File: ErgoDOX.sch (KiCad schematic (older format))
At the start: 62 parts, among them J1 USB, J2 3.5mm, J3 JMP, J4 JMP, SW0:10 SW0:3, SW0:11 SW0:2, SW0:12 SW0:1, SW0:7 SW0:6, SW0:8 SW0:5, SW0:9 SW0:4, SW1:10 SW1:3, SW1:11 SW1:2, SW1:12 SW1:1, SW1:13 SW1:0, SW1:9 SW1:4, SW2:10 SW2:3, SW2:11 SW2:2, SW2:12 SW2:1, SW2:13 SW2:0, SW2:7 SW2:6, SW2:8 SW2:5, SW2:9 SW2:4, SW3:10 SW3:3, SW3:11 SW3:2, SW3:12 SW3:1, SW3:13 SW3:0, SW3:8 SW3:5, SW3:9 SW3:4, SW4:10 SW4:3, SW4:11 SW4:2, SW4:12 SW4:1, SW4:13 SW4:0, SW4:7 SW4:6, SW4:8 SW4:5, SW4:9 SW4:4, SW5:10 SW5:3, SW5:11 SW5:2, SW5:12 SW5:1, SW5:13 SW5:0, SW5:7 SW5:6, SW5:8 SW5:5, SW5:9 SW5:4, U1 ProMicro, U2 MCP23017

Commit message: ...
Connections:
- net VCC: now also U1.26 (VCC); no longer U1.29 (RAW)
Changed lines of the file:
@@
 EESchema Schematic File Version 2
-LIBS:ErgoDOX-rescue
 LIBS:component
 LIBS:74xgxx
@@
 L VCC #PWR015
 U 1 1 500D1293
-P 1950 1300
-F 0 "#PWR015" H 1950 1400 30  0001 C CNN
-F 1 "VCC" H 1950 1400 30  0000 C CNN
-F 2 "" H 1950 1300 60  0001 C CNN
-F 3 "" H 1950 1300 60  0001 C CNN
-	1    1950 1300
-	0    1    1    0
+P 750 3000
+F 0 "#PWR015" H 750 3100 30  0001 C CNN
+F 1 "VCC" H 750 3100 30  0000 C CNN
+F 2 "" H 750 3000 60  0001 C CNN
+F 3 "" H 750 3000 60  0001 C CNN
+	1    750  3000
+	0    -1   -1   0
 $EndComp
 $Comp
@@
 	1    0    0    -1
 $EndComp
-NoConn ~ 750  3000
+NoConn ~ 1950 1300
 $Comp
 L C C1

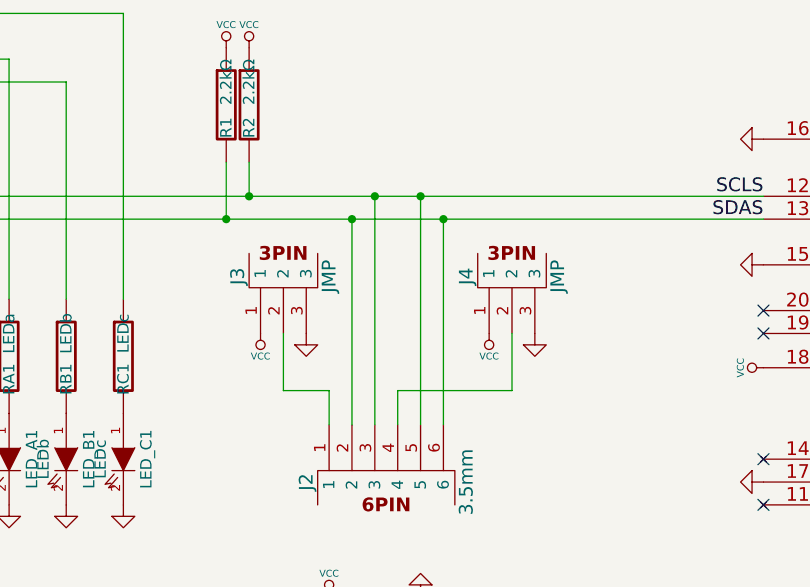
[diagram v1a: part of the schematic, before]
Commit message: Change pin order of 3.5mm jack
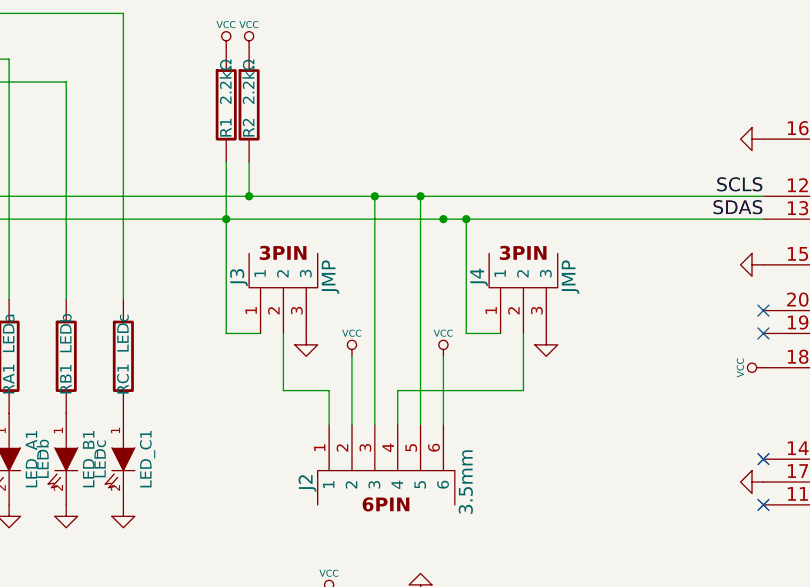
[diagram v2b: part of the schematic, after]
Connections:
- net SDAM: now also J3.1, J4.1; no longer J2.2, J2.6
- net VCC: now also J2.2, J2.6; no longer J3.1, J4.1
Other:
- moved on the sheet: J4
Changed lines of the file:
@@
 L GND #PWR09
 U 1 1 4FD9EC71
-P 5450 3050
-F 0 "#PWR09" H 5450 3050 30  0001 C CNN
-F 1 "GND" H 5450 2980 30  0001 C CNN
-F 2 "" H 5450 3050 60  0001 C CNN
-F 3 "" H 5450 3050 60  0001 C CNN
-	1    5450 3050
+P 5500 3050
+F 0 "#PWR09" H 5500 3050 30  0001 C CNN
+F 1 "GND" H 5500 2980 30  0001 C CNN
+F 2 "" H 5500 3050 60  0001 C CNN
+F 3 "" H 5500 3050 60  0001 C CNN
+	1    5500 3050
 	1    0    0    -1
 $EndComp
 $Comp
 L VCC #PWR010
-U 1 1 4FD9EC77
-P 4250 3000
-F 0 "#PWR010" H 4250 3100 30  0001 C CNN
-F 1 "VCC" H 4250 3100 30  0000 C CNN
-F 2 "" H 4250 3000 60  0001 C CNN
-F 3 "" H 4250 3000 60  0001 C CNN
-	1    4250 3000
-	-1   0    0    1
-$EndComp
-$Comp
-L VCC #PWR011
 U 1 1 4FD9EC7D
-P 5250 3000
-F 0 "#PWR011" H 5250 3100 30  0001 C CNN
-F 1 "VCC" H 5250 3100 30  0000 C CNN
-F 2 "" H 5250 3000 60  0001 C CNN
-F 3 "" H 5250 3000 60  0001 C CNN
-	1    5250 3000
-	-1   0    0    1
+P 4650 3100
+F 0 "#PWR010" H 4650 3200 30  0001 C CNN
+F 1 "VCC" H 4650 3200 30  0000 C CNN
+F 2 "" H 4650 3100 60  0001 C CNN
+F 3 "" H 4650 3100 60  0001 C CNN
+	1    4650 3100
+	1    0    0    -1
 $EndComp
 $Comp
@@
 L 3PIN J4
 U 1 1 4FD9F052
-P 5350 2800
-F 0 "J4" H 5300 3000 60  0000 C CNN
-F 1 "JMP" H 5300 2600 60  0000 C CNN
-F 2 "" H 5350 2800 60  0001 C CNN
-F 3 "" H 5350 2800 60  0001 C CNN
-	1    5350 2800
+P 5400 2800
+F 0 "J4" H 5350 3000 60  0000 C CNN
+F 1 "JMP" H 5350 2600 60  0000 C CNN
+F 2 "" H 5400 2800 60  0001 C CNN
+F 3 "" H 5400 2800 60  0001 C CNN
+	1    5400 2800
 	0    -1   1    0
 $EndComp
@@
 $EndComp
 $Comp
-L VCC #PWR012
+L VCC #PWR011
 U 1 1 4FFF4300
 P 4550 4150
-F 0 "#PWR012" H 4550 4250 30  0001 C CNN
+F 0 "#PWR011" H 4550 4250 30  0001 C CNN
 F 1 "VCC" H 4550 4250 30  0000 C CNN
 F 2 "" H 4550 4150 60  0001 C CNN
@@
 $EndComp
 $Comp
-L GND #PWR013
+L GND #PWR012
 U 1 1 4FFF43E7
 P 4950 4100
-F 0 "#PWR013" H 4950 4100 30  0001 C CNN
+F 0 "#PWR012" H 4950 4100 30  0001 C CNN
 F 1 "GND" H 4950 4030 30  0001 C CNN
 F 2 "" H 4950 4100 60  0001 C CNN
@@
 NoConn ~ 6450 3750
 $Comp
-L GND #PWR014
+L GND #PWR013
 U 1 1 50028213
 P 700 3550
-F 0 "#PWR014" H 700 3550 30  0001 C CNN
+F 0 "#PWR013" H 700 3550 30  0001 C CNN
 F 1 "GND" H 700 3480 30  0001 C CNN
 F 2 "" H 700 3550 60  0001 C CNN
@@
 COL9
 $Comp
-L VCC #PWR015
+L VCC #PWR014
 U 1 1 500D1293
 P 750 3000
-F 0 "#PWR015" H 750 3100 30  0001 C CNN
+F 0 "#PWR014" H 750 3100 30  0001 C CNN
 F 1 "VCC" H 750 3100 30  0000 C CNN
 F 2 "" H 750 3000 60  0001 C CNN
@@
 	1950 2400 6450 2400
 Wire Wire Line
-	5050 2500 5050 3400
-Wire Wire Line
 	4950 2400 4950 3400
 Wire Wire Line
@@
 	4850 3400 4850 3250
 Wire Wire Line
-	4850 3250 5350 3250
-Wire Wire Line
-	5350 3250 5350 3000
+	4850 3250 5400 3250
+Wire Wire Line
+	5400 3250 5400 3000
 Connection ~ 4750 2400
-Connection ~ 4650 2500
 Wire Wire Line
 	3150 1800 3150 2850
@@
 Connection ~ 5050 2500
 Wire Wire Line
-	4100 2250 4100 2500
+	4100 2250 4100 3000
 Connection ~ 4100 2500
 Wire Wire Line
 	4200 2250 4200 2400
 Connection ~ 4200 2400
-Wire Wire Line
-	4650 2500 4650 3400
 Wire Wire Line
 	4750 3400 4750 2400
@@
 	3650 1600 1950 1600
 $Comp
-L GND #PWR016
+L GND #PWR015
 U 1 1 576F2DDE
 P 700 3100
-F 0 "#PWR016" H 700 3100 30  0001 C CNN
+F 0 "#PWR015" H 700 3100 30  0001 C CNN
 F 1 "GND" H 700 3030 30  0001 C CNN
 F 2 "" H 700 3100 60  0000 C CNN
@@
 $EndComp
 $Comp
-L GND #PWR017
+L GND #PWR016
 U 1 1 57617086
 P 6400 2150
-F 0 "#PWR017" H 6400 2150 30  0001 C CNN
+F 0 "#PWR016" H 6400 2150 30  0001 C CNN
 F 1 "GND" H 6400 2080 30  0001 C CNN
 F 2 "" H 6400 2150 60  0001 C CNN
@@
 $EndComp
 $Comp
-L GND #PWR018
+L GND #PWR017
 U 1 1 5761A8AF
 P 6400 3650
-F 0 "#PWR018" H 6400 3650 30  0001 C CNN
+F 0 "#PWR017" H 6400 3650 30  0001 C CNN
 F 1 "GND" H 6400 3580 30  0001 C CNN
 F 2 "" H 6400 3650 60  0001 C CNN
@@
 $EndComp
 $Comp
-L VCC #PWR019
+L VCC #PWR018
 U 1 1 5761B3CF
 P 6450 3150
-F 0 "#PWR019" H 6450 3250 30  0001 C CNN
+F 0 "#PWR018" H 6450 3250 30  0001 C CNN
 F 1 "VCC" H 6450 3250 30  0000 C CNN
 F 2 "" H 6450 3150 60  0000 C CNN
@@
 $EndComp
 $Comp
-L VCC #PWR?
+L VCC #PWR019
 U 1 1 578269AB
 P 10050 2750
-F 0 "#PWR?" H 10050 2850 30  0001 C CNN
+F 0 "#PWR019" H 10050 2850 30  0001 C CNN
 F 1 "VCC" H 10050 2850 30  0000 C CNN
 F 2 "" H 10050 2750 60  0000 C CNN
@@
 $EndComp
 $Comp
-L GND #PWR?
+L GND #PWR020
 U 1 1 57827429
 P 10050 3100
-F 0 "#PWR?" H 10050 3100 30  0001 C CNN
+F 0 "#PWR020" H 10050 3100 30  0001 C CNN
 F 1 "GND" H 10050 3030 30  0001 C CNN
 F 2 "" H 10050 3100 60  0000 C CNN
@@
 	1    0    0    -1
 $EndComp
+Wire Wire Line
+	4100 3000 4250 3000
+Wire Wire Line
+	5300 3000 5150 3000
+Wire Wire Line
+	5150 3000 5150 2500
+Connection ~ 5150 2500
+Wire Wire Line
+	4650 3100 4650 3400
+$Comp
+L VCC #PWR?
+U 1 1 57BF2305
+P 5050 3100
+F 0 "#PWR?" H 5050 3200 30  0001 C CNN
+F 1 "VCC" H 5050 3200 30  0000 C CNN
+F 2 "" H 5050 3100 60  0001 C CNN
+F 3 "" H 5050 3100 60  0001 C CNN
+	1    5050 3100
+	1    0    0    -1
+$EndComp
+Wire Wire Line
+	5050 3400 5050 3100
 $EndSCHEMATC
